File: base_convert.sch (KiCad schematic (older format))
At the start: 10 parts, among them J1 ISP, Q1 Q_PMOS_GSD, SW1 CLEAR, SW2 SELECT, U1 MSP430FR4133IPMR

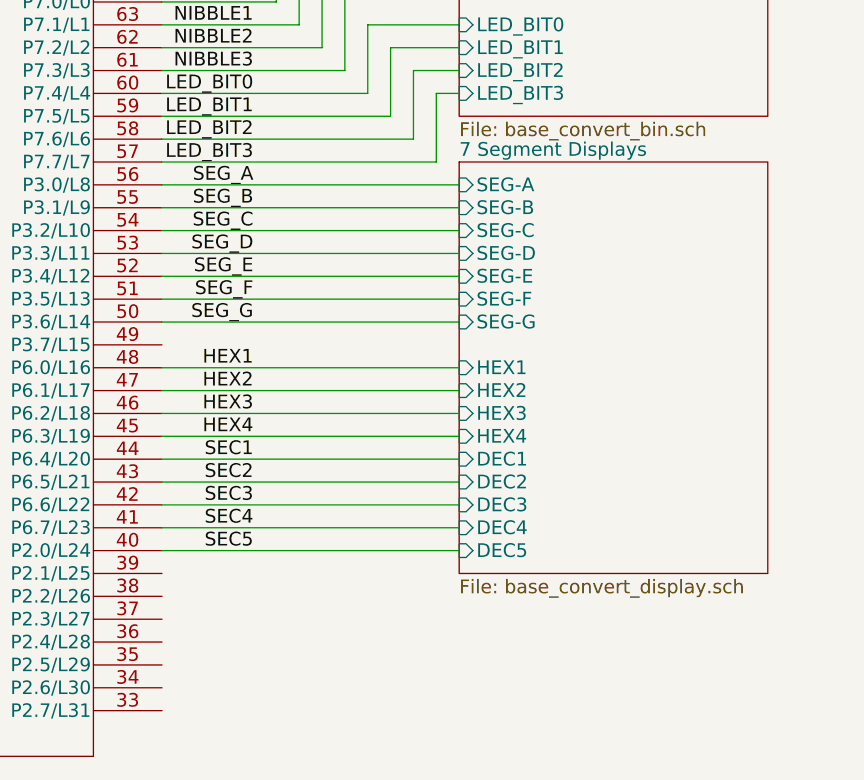
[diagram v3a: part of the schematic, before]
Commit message: update 7-segment display part number
Due to mismatch of display face using a mix of 4 digit and 1 digit displays does not look good. Swtiching all displays to be made up of 2 digit 7-segment display. Decimal display will have extra unused digit.
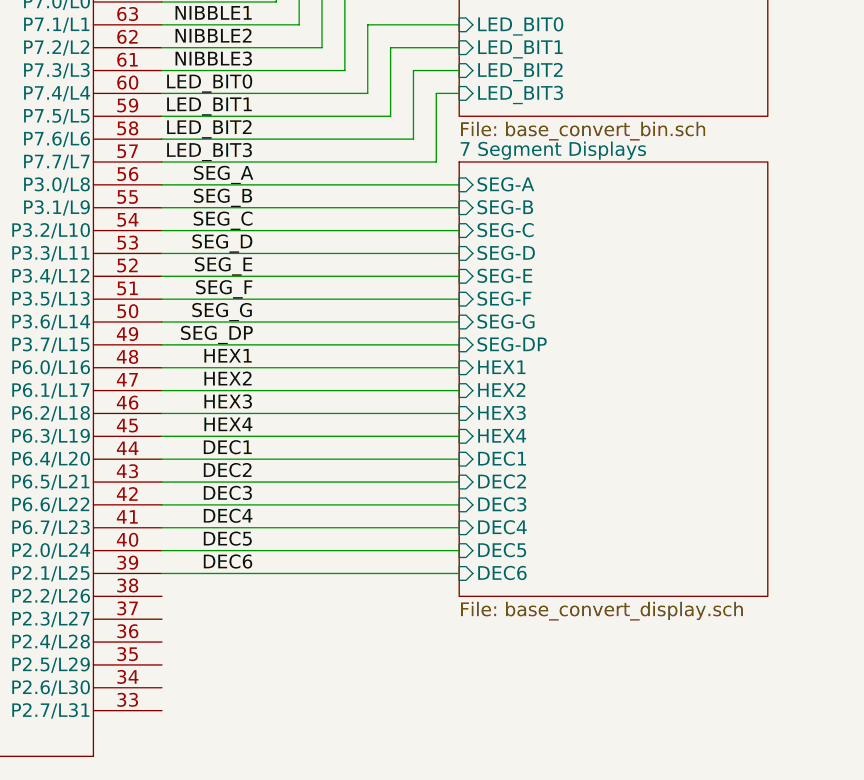
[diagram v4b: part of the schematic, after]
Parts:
- SW2: footprint (none) -> Switch_CK:DP4T_SS-24E06-TG5P
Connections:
- net DEC6: now reaches U1.39 (P2.1/L25)
- net SEG_DP: now reaches U1.49 (P3.7/L15)
- net SEC1 renamed DEC1
- net SEC2 renamed DEC2
- net SEC3 renamed DEC3
- net SEC4 renamed DEC4
- net SEC5 renamed DEC5
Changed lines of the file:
@@
 $EndDescr
 $Sheet
-S 8600 3650 1350 1800
+S 8600 3650 1350 1900
 U 5AEA74C1
 F0 "7 Segment Displays" 60
@@
 F16 "SEG-F" I L 8600 4250 60
 F17 "SEG-G" I L 8600 4350 60
+F18 "DEC6" I L 8600 5450 60
+F19 "SEG-DP" I L 8600 4450 60
 $EndSheet
 $Comp
@@
 $EndComp
 $Comp
-L GND #PWR01
+L GND #PWR3
 U 1 1 5AEC3D6F
 P 1000 1600
-F 0 "#PWR01" H 1000 1350 50  0001 C CNN
+F 0 "#PWR3" H 1000 1350 50  0001 C CNN
 F 1 "GND" H 1000 1450 50  0000 C CNN
 F 2 "" H 1000 1600 50  0001 C CNN
@@
 	1000 1550 1000 1600
 $Comp
-L GND #PWR02
+L GND #PWR5
 U 1 1 5AEC5CE6
 P 2450 1700
-F 0 "#PWR02" H 2450 1450 50  0001 C CNN
+F 0 "#PWR5" H 2450 1450 50  0001 C CNN
 F 1 "GND" H 2450 1550 50  0000 C CNN
 F 2 "" H 2450 1700 50  0001 C CNN
@@
 	2450 1700 2450 1500
 $Comp
-L VCC #PWR03
+L VCC #PWR7
 U 1 1 5AEC60F4
 P 2950 1100
-F 0 "#PWR03" H 2950 950 50  0001 C CNN
+F 0 "#PWR7" H 2950 950 50  0001 C CNN
 F 1 "VCC" H 2950 1250 50  0000 C CNN
 F 2 "" H 2950 1100 50  0001 C CNN
@@
 	2450 3650 2450 4200
 $Comp
-L GND #PWR04
+L GND #PWR6
 U 1 1 5AF08A85
 P 2450 4200
-F 0 "#PWR04" H 2450 3950 50  0001 C CNN
+F 0 "#PWR6" H 2450 3950 50  0001 C CNN
 F 1 "GND" H 2450 4050 50  0000 C CNN
 F 2 "" H 2450 4200 50  0001 C CNN
@@
 Connection ~ 2450 4150
 $Comp
-L VCC #PWR05
+L VCC #PWR4
 U 1 1 5AF0BA91
 P 1850 3700
-F 0 "#PWR05" H 1850 3550 50  0001 C CNN
+F 0 "#PWR4" H 1850 3550 50  0001 C CNN
 F 1 "VCC" H 1850 3850 50  0000 C CNN
 F 2 "" H 1850 3700 50  0001 C CNN
@@
 F 0 "SW2" H 1200 3420 50  0000 C CNN
 F 1 "SELECT" H 1200 2650 50  0000 C CNN
-F 2 "" H 1200 3250 50  0001 C CNN
+F 2 "Switch_CK:DP4T_SS-24E06-TG5P" H 1200 3250 50  0001 C CNN
 F 3 "" H 1200 3250 50  0001 C CNN
 F 4 "NONE" H 1200 3050 60  0001 C CNN "Manufacture"
@@
 	1400 3350 2850 3350
 $Comp
-L GND #PWR06
+L GND #PWR2
 U 1 1 5AF24AED
 P 750 3300
-F 0 "#PWR06" H 750 3050 50  0001 C CNN
+F 0 "#PWR2" H 750 3050 50  0001 C CNN
 F 1 "GND" H 750 3150 50  0000 C CNN
 F 2 "" H 750 3300 50  0001 C CNN
@@
 $EndComp
 $Comp
-L GND #PWR07
+L GND #PWR8
 U 1 1 5AF3048A
 P 2950 2050
-F 0 "#PWR07" H 2950 1800 50  0001 C CNN
+F 0 "#PWR8" H 2950 1800 50  0001 C CNN
 F 1 "GND" H 2950 1900 50  0000 C CNN
 F 2 "" H 2950 2050 50  0001 C CNN
@@
 	5550 1150 5550 1000
 $Comp
-L GND #PWR08
+L GND #PWR10
 U 1 1 5AF42179
 P 5550 1600
-F 0 "#PWR08" H 5550 1350 50  0001 C CNN
+F 0 "#PWR10" H 5550 1350 50  0001 C CNN
 F 1 "GND" H 5550 1450 50  0000 C CNN
 F 2 "" H 5550 1600 50  0001 C CNN
@@
 	5550 1450 5550 1600
 $Comp
-L VCC #PWR09
+L VCC #PWR9
 U 1 1 5AF43264
 P 5550 1000
-F 0 "#PWR09" H 5550 850 50  0001 C CNN
+F 0 "#PWR9" H 5550 850 50  0001 C CNN
 F 1 "VCC" H 5550 1150 50  0000 C CNN
 F 2 "" H 5550 1000 50  0001 C CNN
@@
 	1250 3750 1550 3750
 $Comp
-L GND #PWR010
+L GND #PWR1
 U 1 1 5AF596D6
 P 700 4250
-F 0 "#PWR010" H 700 4000 50  0001 C CNN
+F 0 "#PWR1" H 700 4000 50  0001 C CNN
 F 1 "GND" H 700 4100 50  0000 C CNN
 F 2 "" H 700 4250 50  0001 C CNN
@@
 Text Label 7700 4850 2    60   ~ 0
 HEX4
+Wire Wire Line
+	8600 5450 7300 5450
+Wire Wire Line
+	8600 4450 7300 4450
+Text Label 7700 4450 2    60   ~ 0
+SEG_DP
 Text Label 7700 4950 2    60   ~ 0
-SEC1
+DEC1
 Text Label 7700 5050 2    60   ~ 0
-SEC2
+DEC2
 Text Label 7700 5150 2    60   ~ 0
-SEC3
+DEC3
 Text Label 7700 5250 2    60   ~ 0
-SEC4
+DEC4
 Text Label 7700 5350 2    60   ~ 0
-SEC5
+DEC5
+Text Label 7700 5450 2    60   ~ 0
+DEC6
 $EndSCHEMATC

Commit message: updated shema fields. Raplced tack switch with 4 pin footprint
Using 4 pin tack switch to ease pcb layout connecitions. Also updated component fields in schema
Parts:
- BT1: value Battery -> 2x AA Battery; Description NONE -> HOLDER BATT 2-AA CELLS PC MNT; Manufacture NONE -> MPD (Memory Protection Devices); Mfg Part Number NONE -> BC2AAPC; Package NONE -> PC Pin
- C1, C2, R1, R2, SW2: Description NONE -> (none); Manufacture NONE -> (none); Mfg Part Number NONE -> (none); Package NONE -> (none)
- SW1: footprint Buttons_Switches_THT:SW_PUSH_6mm -> Buttons_Switches_THT:SW_TH_Tactile_Omron_B3F-10xx; symbol SW_Push -> SW_Push_Dual; Description NONE -> (none); Manufacture NONE -> (none); Mfg Part Number NONE -> (none); Package NONE -> (none)
- U1: Description (none) -> IC MCU 16BIT 15.5KB FRAM 64LQFP; Manufacture (none) -> Texas Instruments; Mfg Part Number (none) -> MSP430FR4133IPMR; Package (none) -> 64-LQFP (10x10)

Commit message: Push and shove for the win!
To Do: clean up.
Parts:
- SW1: symbol SW_Push_Dual -> SW_Push_Dual2; Description (none) -> NONE; Manufacture (none) -> NONE; Mfg Part Number (none) -> NONE; Package (none) -> NONE
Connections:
- net labels removed: DEC1, DEC2, DEC3, DEC4, DEC5, DEC6, HEX1, HEX2, HEX3, HEX4, LED_BIT0, LED_BIT1, LED_BIT2, LED_BIT3, NIBBLE0, NIBBLE1, NIBBLE2, NIBBLE3, SEG_A, SEG_B, SEG_C, SEG_D, SEG_DP, SEG_E, SEG_F, SEG_G
- wire segments 104 -> 106
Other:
- moved on the sheet: Q1, R1, R2, SW2A, SW2B

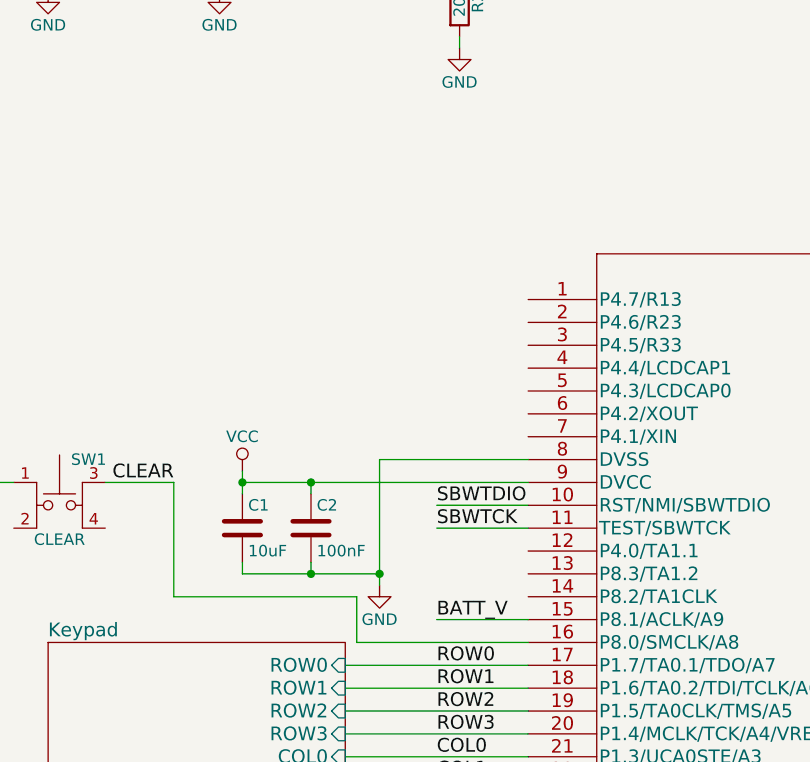
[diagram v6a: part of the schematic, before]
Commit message: add header to break out 3 unsused pins just in case
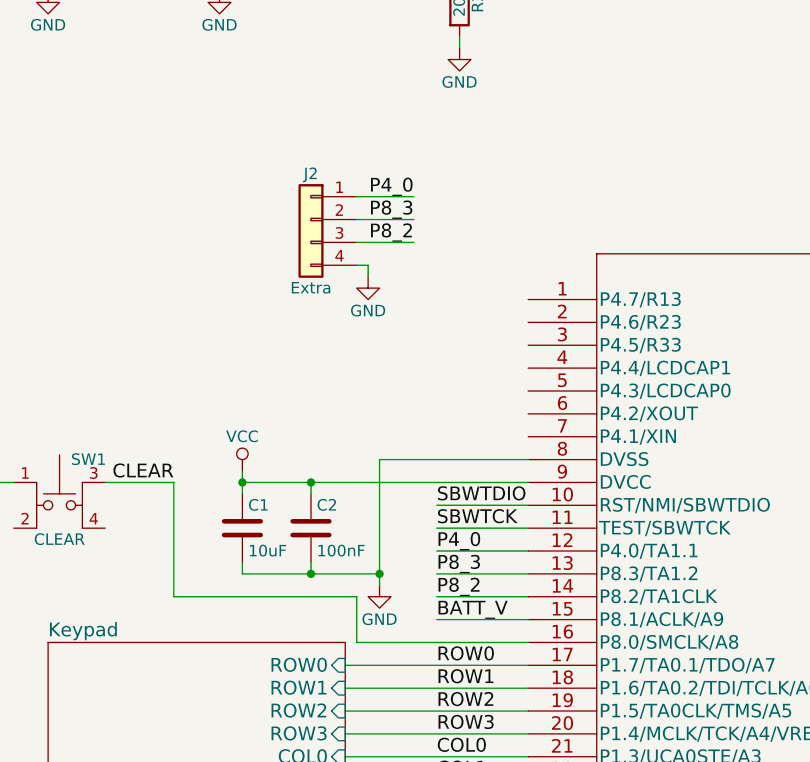
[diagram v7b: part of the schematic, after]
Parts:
- added J2: Extra, Pin_Headers:Pin_Header_Straight_1x04_Pitch2.54mm, symbol Conn_01x04
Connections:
- net GND: now also J2.4 (Pin_4)
- net P4_0: now reaches U1.12 (P4.0/TA1.1)
- net P4_0: now also J2.1 (Pin_1)
- net P8_3: now reaches U1.13 (P8.3/TA1.2)
- net P8_3: now also J2.2 (Pin_2)
- net P8_2: now reaches U1.14 (P8.2/TA1CLK)
- net P8_2: now also J2.3 (Pin_3)
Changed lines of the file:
@@
 $EndComp
 $Comp
-L GND #PWR01
+L GND #PWR2
 U 1 1 5AEC3D6F
 P 1000 1600
-F 0 "#PWR01" H 1000 1350 50  0001 C CNN
+F 0 "#PWR2" H 1000 1350 50  0001 C CNN
 F 1 "GND" H 1000 1450 50  0000 C CNN
 F 2 "" H 1000 1600 50  0001 C CNN
@@
 $EndComp
 $Comp
-L GND #PWR02
+L GND #PWR3
 U 1 1 5AEC5CE6
 P 1750 1600
-F 0 "#PWR02" H 1750 1350 50  0001 C CNN
+F 0 "#PWR3" H 1750 1350 50  0001 C CNN
 F 1 "GND" H 1750 1450 50  0000 C CNN
 F 2 "" H 1750 1600 50  0001 C CNN
@@
 $EndComp
 $Comp
-L VCC #PWR03
+L VCC #PWR7
 U 1 1 5AEC60F4
 P 2800 900
-F 0 "#PWR03" H 2800 750 50  0001 C CNN
+F 0 "#PWR7" H 2800 750 50  0001 C CNN
 F 1 "VCC" H 2800 1050 50  0000 C CNN
 F 2 "" H 2800 900 50  0001 C CNN
@@
 $EndComp
 $Comp
-L GND #PWR04
+L GND #PWR6
 U 1 1 5AF08A85
 P 2450 4200
-F 0 "#PWR04" H 2450 3950 50  0001 C CNN
+F 0 "#PWR6" H 2450 3950 50  0001 C CNN
 F 1 "GND" H 2450 4050 50  0000 C CNN
 F 2 "" H 2450 4200 50  0001 C CNN
@@
 $EndComp
 $Comp
-L VCC #PWR05
+L VCC #PWR4
 U 1 1 5AF0BA91
 P 1850 3700
-F 0 "#PWR05" H 1850 3550 50  0001 C CNN
+F 0 "#PWR4" H 1850 3550 50  0001 C CNN
 F 1 "VCC" H 1850 3850 50  0000 C CNN
 F 2 "" H 1850 3700 50  0001 C CNN
@@
 $EndComp
 $Comp
-L GND #PWR06
+L GND #PWR11
 U 1 1 5AF24AED
 P 9750 6400
-F 0 "#PWR06" H 9750 6150 50  0001 C CNN
+F 0 "#PWR11" H 9750 6150 50  0001 C CNN
 F 1 "GND" H 9750 6250 50  0000 C CNN
 F 2 "" H 9750 6400 50  0001 C CNN
@@
 $EndComp
 $Comp
-L GND #PWR07
+L GND #PWR8
 U 1 1 5AF3048A
 P 2800 1850
-F 0 "#PWR07" H 2800 1600 50  0001 C CNN
+F 0 "#PWR8" H 2800 1600 50  0001 C CNN
 F 1 "GND" H 2800 1700 50  0000 C CNN
 F 2 "" H 2800 1850 50  0001 C CNN
@@
 $EndComp
 $Comp
-L GND #PWR08
+L GND #PWR10
 U 1 1 5AF42179
 P 5550 1600
-F 0 "#PWR08" H 5550 1350 50  0001 C CNN
+F 0 "#PWR10" H 5550 1350 50  0001 C CNN
 F 1 "GND" H 5550 1450 50  0000 C CNN
 F 2 "" H 5550 1600 50  0001 C CNN
@@
 $EndComp
 $Comp
-L VCC #PWR09
+L VCC #PWR9
 U 1 1 5AF43264
 P 5550 1000
-F 0 "#PWR09" H 5550 850 50  0001 C CNN
+F 0 "#PWR9" H 5550 850 50  0001 C CNN
 F 1 "VCC" H 5550 1150 50  0000 C CNN
 F 2 "" H 5550 1000 50  0001 C CNN
@@
 $EndComp
 $Comp
-L GND #PWR010
+L GND #PWR1
 U 1 1 5AF596D6
 P 700 4250
-F 0 "#PWR010" H 700 4000 50  0001 C CNN
+F 0 "#PWR1" H 700 4000 50  0001 C CNN
 F 1 "GND" H 700 4100 50  0000 C CNN
 F 2 "" H 700 4250 50  0001 C CNN
@@
 Wire Wire Line
 	7650 5850 7300 5850
+$Comp
+L Conn_01x04 J2
+U 1 1 5AFB5A51
+P 2150 2600
+F 0 "J2" H 2150 2800 50  0000 C CNN
+F 1 "Extra" H 2150 2300 50  0000 C CNN
+F 2 "Pin_Headers:Pin_Header_Straight_1x04_Pitch2.54mm" H 2150 2600 50  0001 C CNN
+F 3 "" H 2150 2600 50  0001 C CNN
+F 4 "NONE" H 2150 2600 60  0001 C CNN "Manufacture"
+F 5 "NONE" H 2150 2600 60  0001 C CNN "Mfg Part Number"
+F 6 "NONE" H 2150 2600 60  0001 C CNN "Package"
+F 7 "NONE" H 2150 2600 60  0001 C CNN "Description"
+	1    2150 2600
+	-1   0    0    -1
+$EndComp
+Wire Wire Line
+	3100 4050 2700 4050
+Wire Wire Line
+	3100 4150 2700 4150
+Wire Wire Line
+	3100 4250 2700 4250
+Text Label 2700 4050 0    60   ~ 0
+P4_0
+Text Label 2700 4150 0    60   ~ 0
+P8_3
+Text Label 2700 4250 0    60   ~ 0
+P8_2
+Text Label 2600 2500 2    60   ~ 0
+P4_0
+Text Label 2600 2600 2    60   ~ 0
+P8_3
+Text Label 2600 2700 2    60   ~ 0
+P8_2
+Wire Wire Line
+	2600 2500 2350 2500
+Wire Wire Line
+	2600 2600 2350 2600
+Wire Wire Line
+	2600 2700 2350 2700
+$Comp
+L GND #PWR5
+U 1 1 5AFB7D7E
+P 2400 2850
+F 0 "#PWR5" H 2400 2600 50  0001 C CNN
+F 1 "GND" H 2400 2700 50  0000 C CNN
+F 2 "" H 2400 2850 50  0001 C CNN
+F 3 "" H 2400 2850 50  0001 C CNN
+	1    2400 2850
+	1    0    0    -1
+$EndComp
+Wire Wire Line
+	2350 2800 2400 2800
+Wire Wire Line
+	2400 2800 2400 2850
 $EndSCHEMATC
